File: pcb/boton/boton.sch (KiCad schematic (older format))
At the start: 4 parts, among them J1 RJ45, P1 CONN_6

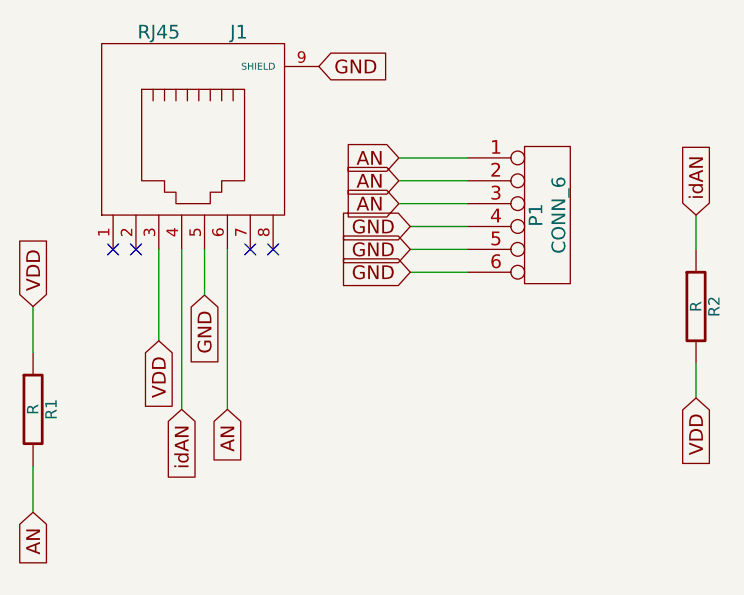
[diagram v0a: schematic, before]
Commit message: New version botton PBC compatible with 5x5mm connector
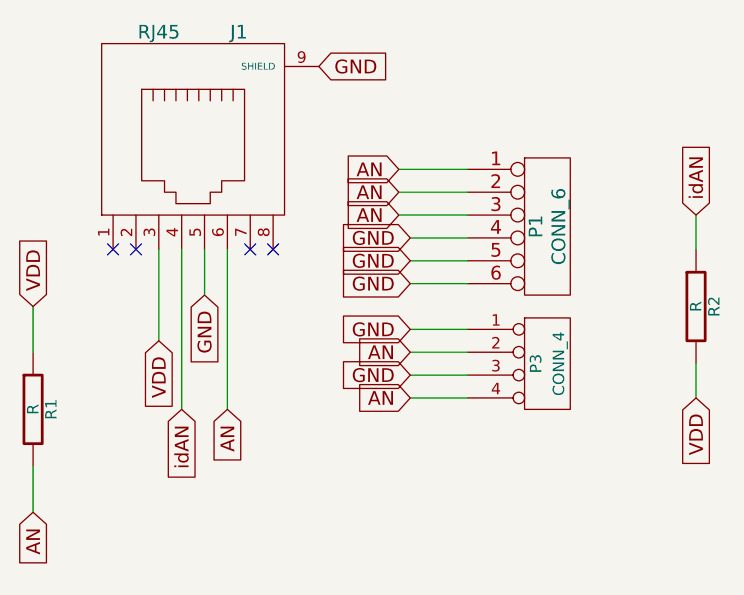
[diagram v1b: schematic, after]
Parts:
- added P3: CONN_4, symbol CONN_4
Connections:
- net AN: now also P3.2 (P2), P3.4 (P4)
- net GND: now also P3.1 (P1), P3.3 (P3)
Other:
- moved on the sheet: P1
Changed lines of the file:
@@
-EESchema Schematic File Version 2  date lun 14 may 2012 12:02:10 UYT
+EESchema Schematic File Version 2  date jue 21 jun 2012 16:05:26 UYT
 LIBS:power
 LIBS:device
@@
 Sheet 1 1
 Title ""
-Date "14 may 2012"
+Date "21 jun 2012"
 Rev ""
 Comp ""
@@
 $EndDescr
 Wire Wire Line
-	3550 2050 3300 2050
+	3300 2600 3550 2600
 Wire Wire Line
-	3300 1850 3550 1850
+	3300 2400 3550 2400
+Wire Wire Line
+	3550 2100 3300 2100
+Wire Wire Line
+	3300 1900 3550 1900
 Wire Wire Line
 	4550 1950 4550 1800
@@
 	4550 2450 4550 2600
 Wire Wire Line
-	3250 1550 3550 1550
+	3250 1600 3550 1600
 Wire Wire Line
-	3250 1650 3550 1650
+	3250 1700 3550 1700
 Wire Wire Line
-	3250 1750 3550 1750
+	3250 1800 3550 1800
 Wire Wire Line
-	3550 1950 3300 1950
-Text GLabel 3300 2050 0    60   Input ~ 0
+	3550 2000 3300 2000
+Wire Wire Line
+	3300 2300 3550 2300
+Wire Wire Line
+	3300 2500 3550 2500
+Text GLabel 3300 2600 0    60   Input ~ 0
+AN
+Text GLabel 3300 2400 0    60   Input ~ 0
+AN
+Text GLabel 3300 2500 0    60   Input ~ 0
 GND
-Text GLabel 3300 1950 0    60   Input ~ 0
+Text GLabel 3300 2300 0    60   Input ~ 0
 GND
-Text GLabel 3250 1750 0    60   Input ~ 0
+$Comp
+L CONN_4 P3
+U 1 1 4FE36678
+P 3900 2450
+F 0 "P3" V 3850 2450 50  0000 C CNN
+F 1 "CONN_4" V 3950 2450 50  0000 C CNN
+	1    3900 2450
+	1    0    0    -1
+$EndComp
+Text GLabel 3300 2100 0    60   Input ~ 0
+GND
+Text GLabel 3300 2000 0    60   Input ~ 0
+GND
+Text GLabel 3250 1800 0    60   Input ~ 0
 AN
-Text GLabel 3250 1650 0    60   Input ~ 0
+Text GLabel 3250 1700 0    60   Input ~ 0
 AN
-Text GLabel 3250 1550 0    60   Input ~ 0
+Text GLabel 3250 1600 0    60   Input ~ 0
 AN
 $Comp
 L CONN_6 P1
 U 1 1 4FB11C28
-P 3900 1800
-F 0 "P1" V 3850 1800 60  0000 C CNN
-F 1 "CONN_6" V 3950 1800 60  0000 C CNN
-	1    3900 1800
+P 3900 1850
+F 0 "P1" V 3850 1850 60  0000 C CNN
+F 1 "CONN_6" V 3950 1850 60  0000 C CNN
+	1    3900 1850
 	1    0    0    -1
 $EndComp
-Text GLabel 3300 1850 0    60   Input ~ 0
+Text GLabel 3300 1900 0    60   Input ~ 0
 GND
 Text GLabel 1650 3100 3    60   Input ~ 0

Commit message: boton compatibility with sw 12mm version 1.2
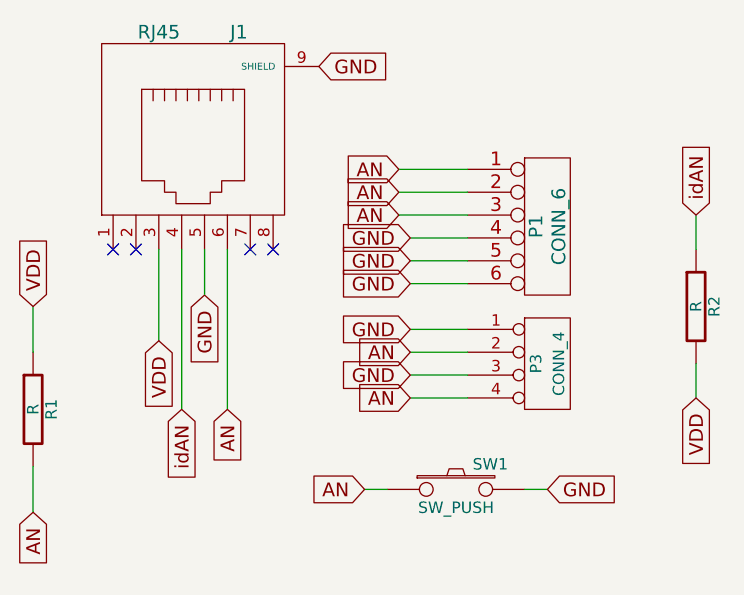
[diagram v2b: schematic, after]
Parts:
- added SW1: SW_PUSH, symbol SW_PUSH
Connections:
- net AN: now also SW1.1
- net GND: now also SW1.2
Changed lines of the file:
@@
-EESchema Schematic File Version 2  date jue 21 jun 2012 16:05:26 UYT
+EESchema Schematic File Version 2  date jue 02 may 2013 11:32:49 UYT
 LIBS:power
 LIBS:device
@@
 Sheet 1 1
 Title ""
-Date "21 jun 2012"
+Date "2 may 2013"
 Rev ""
 Comp ""
@@
 Comment4 ""
 $EndDescr
+Wire Wire Line
+	3200 3000 3100 3000
 Wire Wire Line
 	3300 2600 3550 2600
@@
 Wire Wire Line
 	3300 2500 3550 2500
+Wire Wire Line
+	3800 3000 3900 3000
+Text GLabel 3900 3000 2    60   Input ~ 0
+GND
+Text GLabel 3100 3000 0    60   Input ~ 0
+AN
+$Comp
+L SW_PUSH SW1
+U 1 1 51826E72
+P 3500 3000
+F 0 "SW1" H 3650 3110 50  0000 C CNN
+F 1 "SW_PUSH" H 3500 2920 50  0000 C CNN
+	1    3500 3000
+	1    0    0    -1
+$EndComp
 Text GLabel 3300 2600 0    60   Input ~ 0
 AN
